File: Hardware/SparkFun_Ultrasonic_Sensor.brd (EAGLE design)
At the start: 45 x 21.5 mm, 61 parts, among them J4 Vertical Qwiic Connector, J6 Vertical Qwiic Connector, Q1 600mA/40V, U5 ULTRASONIC_SENSOR_TRANSMITTER, U6 LMV324, U7 STM8L051F3, U8 SP3232EB, U9 ULTRASONIC_SENSOR_RECEIVER

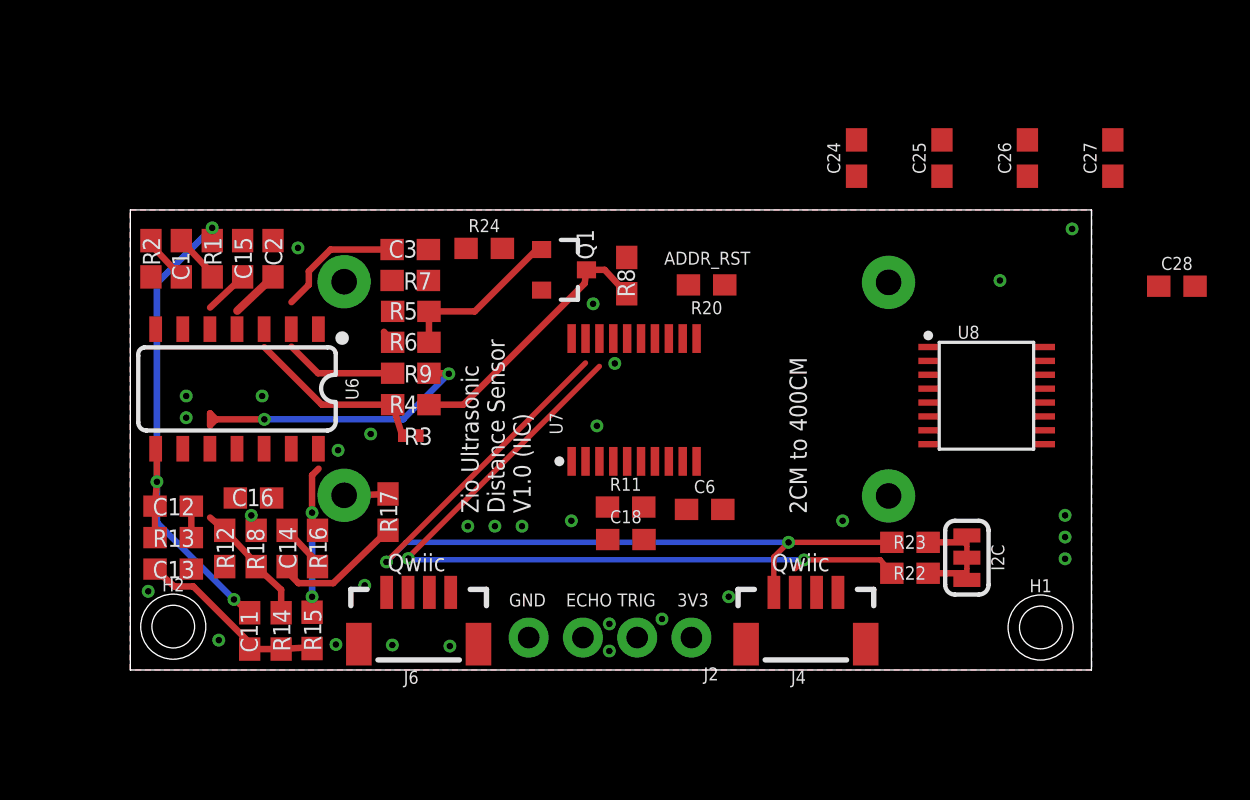
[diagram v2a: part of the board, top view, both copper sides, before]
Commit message: Moves passives around the PCB
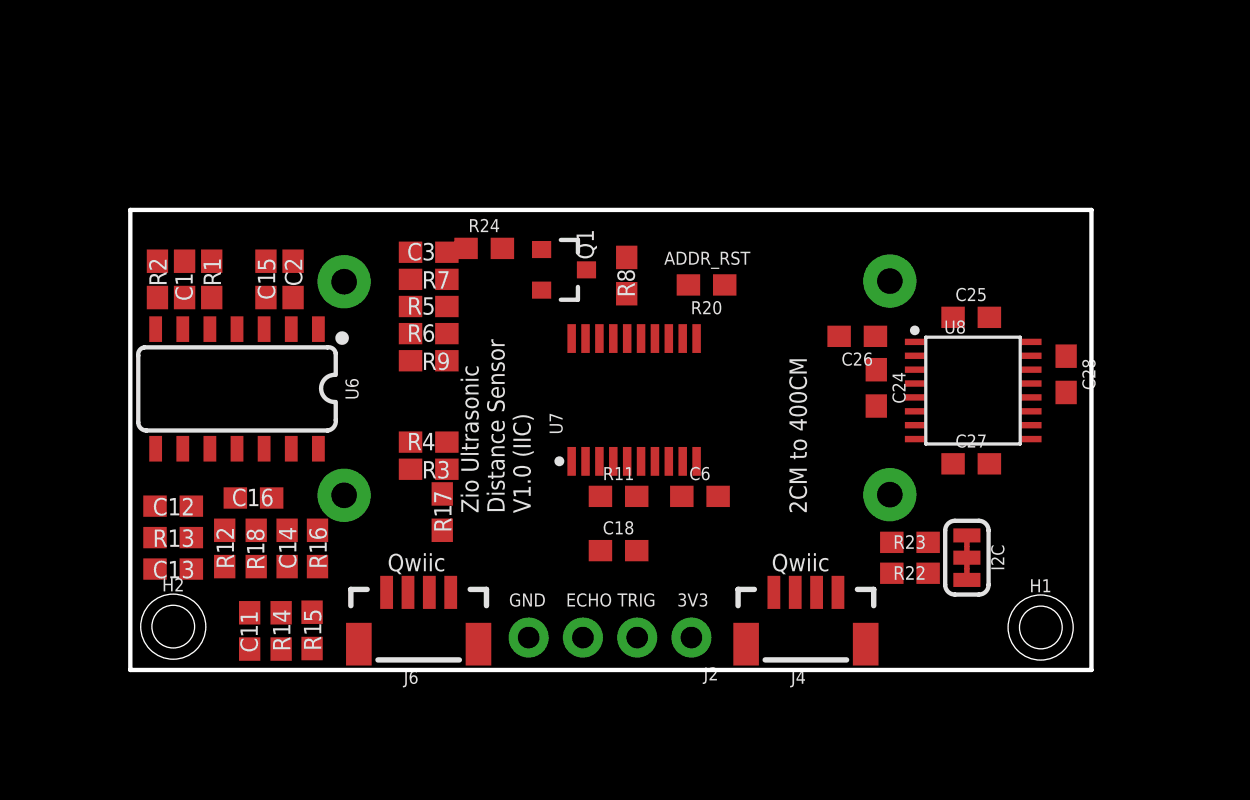
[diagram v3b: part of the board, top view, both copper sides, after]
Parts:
- R3: value 4.3k -> 4.7k; device SparkFun-Resistors:0402_MURATA -> SparkFun-Resistors:0603
- moved C27 15.8 mm to (39.4, 11.7), turned to 0 degrees
- moved C26 11.5 mm to (34.0, 17.7), turned to 180 degrees
- moved C24 10.8 mm to (34.9, 15.2), turned to 270 degrees
- moved C25 7.58 mm to (39.4, 18.5), turned to 0 degrees
- moved C28 6.63 mm to (43.8, 15.9), turned to 270 degrees
- moved R17 2.54 mm to (14.6, 9.42)
- moved R4 1.94 mm to (14.0, 12.7)
- moved R3 1.78 mm to (14.0, 11.4)
- moved C15 1.46 mm to (6.35, 20.3)
- moved C2 1.35 mm to (7.62, 20.3)
- moved R9 1.02 mm to (14.0, 16.5)
- moved R2 1.01 mm to (1.27, 20.3)
- moved C1 0.98 mm to (2.54, 20.3)
- moved R1 0.97 mm to (3.81, 20.3)
- moved R6 0.93 mm to (14.0, 17.8)
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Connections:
- net N$1: now also R3.1; no longer R3.P$1
- net N$4: now also R3.2; no longer R3.P$2
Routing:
- net SCL: track 39.8 -> 0.00 mm, vias 2 -> 0
- net SDA: track 36.3 -> 0.00 mm, vias 2 -> 0
- net N$10: track 25.4 -> 0.00 mm, vias 3 -> 0
- net N$31: track 22.5 -> 0.00 mm, vias 2 -> 0
- net INT: track 12.7 -> 0.00 mm
- net PB4: track 11.4 -> 0.00 mm
- net N$12: track 9.10 -> 0.00 mm
- net N$4: track 8.64 -> 0.00 mm
- net N$5: track 7.92 -> 0.00 mm
- net N$14: track 7.81 -> 0.00 mm, vias 2 -> 0
- net N$16: track 6.19 -> 0.00 mm
- net N$15: track 2.50 -> 0.00 mm
- net N$2: track 2.34 -> 0.00 mm
- net 3.3V: track 2.31 -> 0.00 mm
- net N$3: track 2.27 -> 0.00 mm
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
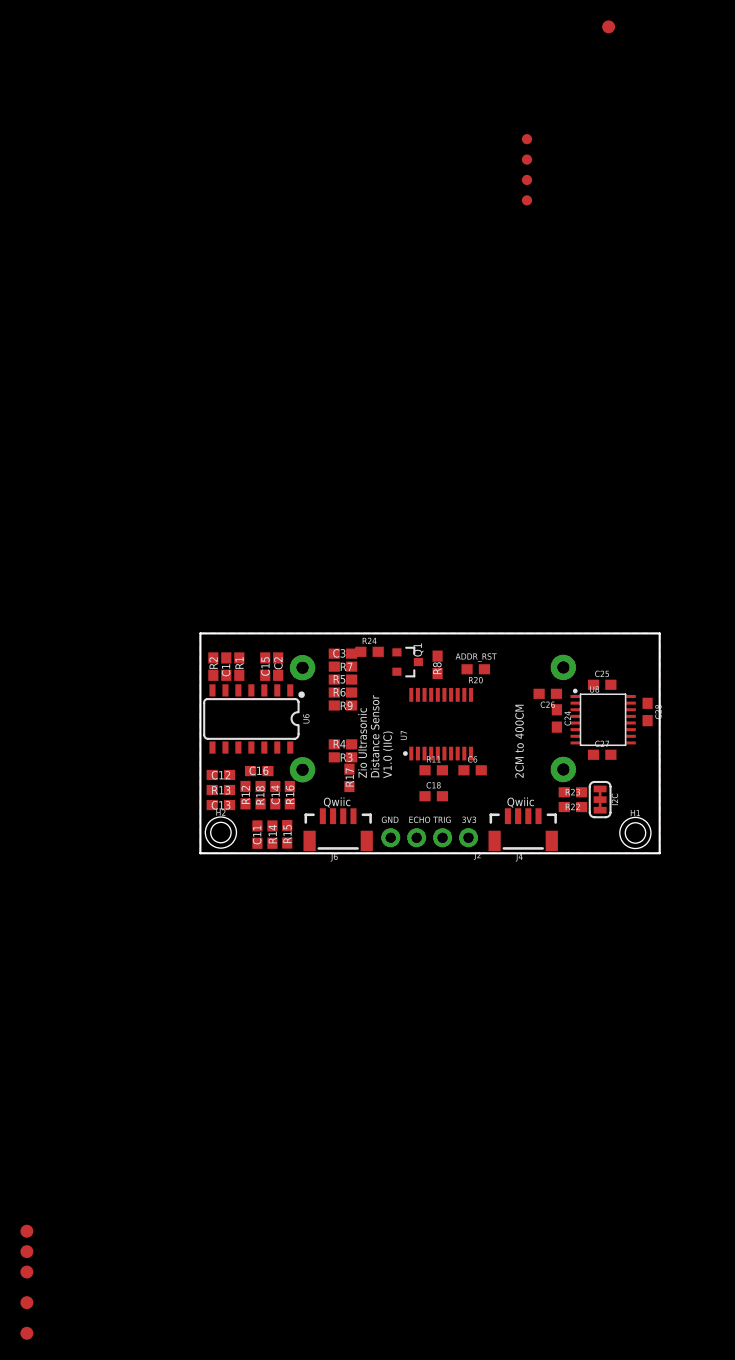
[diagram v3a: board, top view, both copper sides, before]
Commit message: Moves design to origin, routes most signals
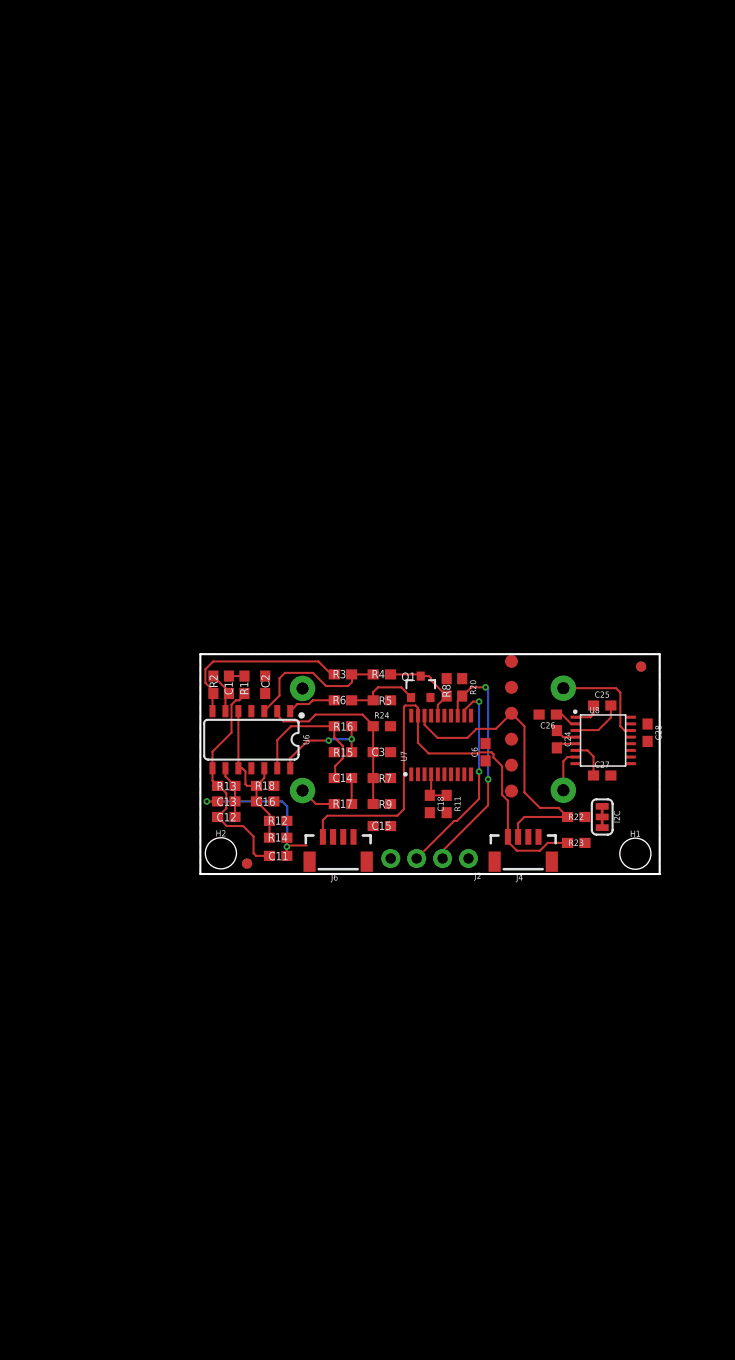
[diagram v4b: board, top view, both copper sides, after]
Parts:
- removed U$5: (no value), ZIO_silkscreen_package:6MM
- moved TP5 76.7 mm to (30.5, 18.3)
- moved FD1 76.1 mm to (4.57, 1.02), turned to 90 degrees
- moved TP6 75.1 mm to (30.5, 13.2)
- moved TP4 72.5 mm to (30.5, 15.7)
- moved FD4 70.5 mm to (4.57, 1.02), flipped to the bottom, turned to 90 degrees
- moved TP2 65.9 mm to (30.5, 10.7)
- moved TP3 65.5 mm to (30.5, 8.13)
- moved TP1 62.9 mm to (30.5, 20.8)
- moved FD2 50.9 mm to (43.2, 20.3), turned to 90 degrees
- moved FD3 49.0 mm to (43.2, 20.3), flipped to the bottom, turned to 90 degrees
- moved FRAME1 21.6 mm to (-7.16, -13.9)
- moved C15 19.4 mm to (17.8, 4.70), turned to 0 degrees
- moved R7 11.6 mm to (17.8, 9.40)
- moved R9 10.4 mm to (17.8, 6.86)
- moved C3 10.4 mm to (17.8, 11.9)
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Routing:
- net SCL: track 0.00 -> 48.7 mm
- net SDA: track 0.00 -> 30.9 mm
- net TRIG: track 0.00 -> 23.5 mm, vias 0 -> 2
- net N$10: track 0.00 -> 22.2 mm
- net ECHO: track 0.00 -> 20.4 mm, vias 0 -> 2
- net PB4: track 0.00 -> 18.5 mm
- net N$1: track 0.00 -> 17.9 mm
- net N$12: track 0.00 -> 16.9 mm, vias 0 -> 2
- net N$31: track 0.00 -> 16.5 mm
- net N$4: track 0.00 -> 14.7 mm
- net N$15: track 0.00 -> 14.7 mm
- net N$14: track 0.00 -> 10.3 mm, vias 0 -> 2
- net N$48: track 0.00 -> 10.3 mm
- net INT: track 0.00 -> 8.78 mm
- net N$5: track 0.00 -> 7.26 mm
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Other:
- board text removed: "2CM to 400CM"
- board text removed: "3V3"
- board text removed: "ADDR_RST"
- board text removed: "ECHO"
- board text removed: "GND"
- board text removed: "Qwiic"
- board text removed: "TRIG"
- board text removed: "Zio Ultrasonic Distance Sensor V1.0 (IIC)"

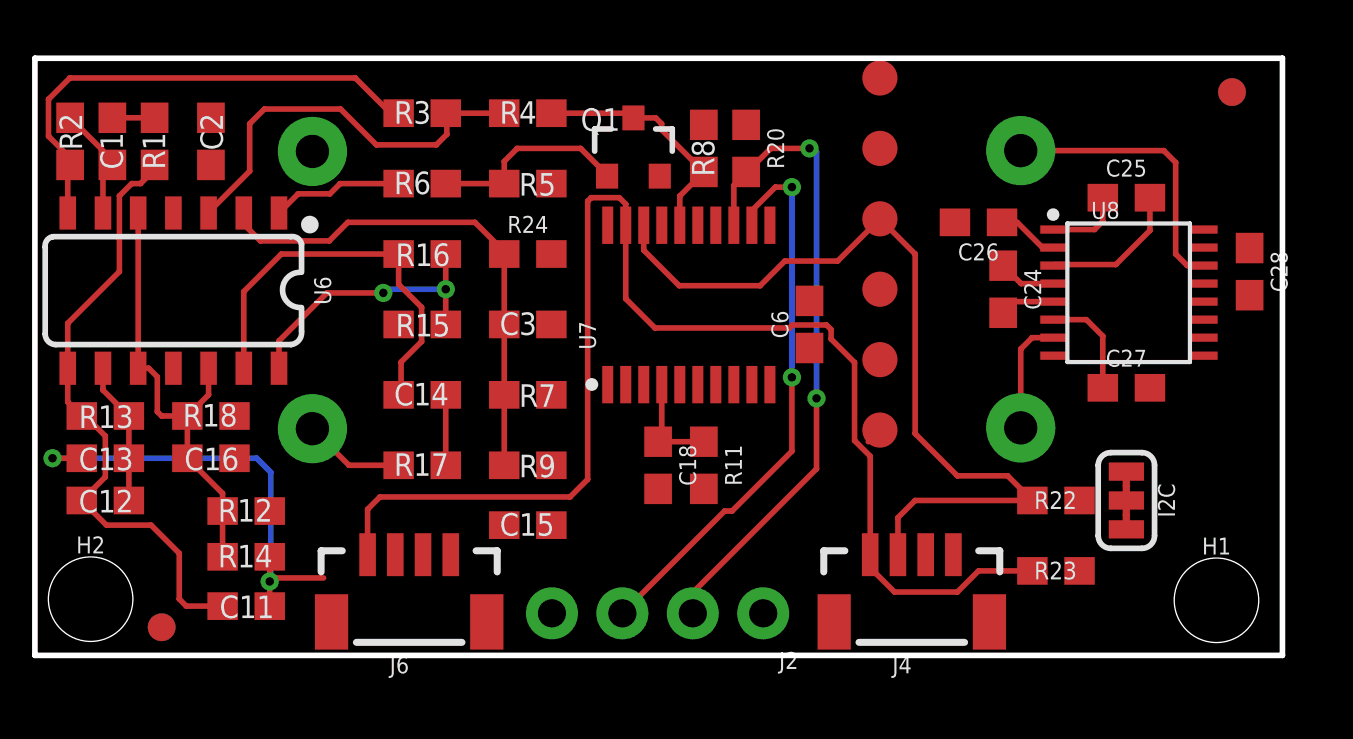
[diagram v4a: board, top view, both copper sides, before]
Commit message: Routes more wires
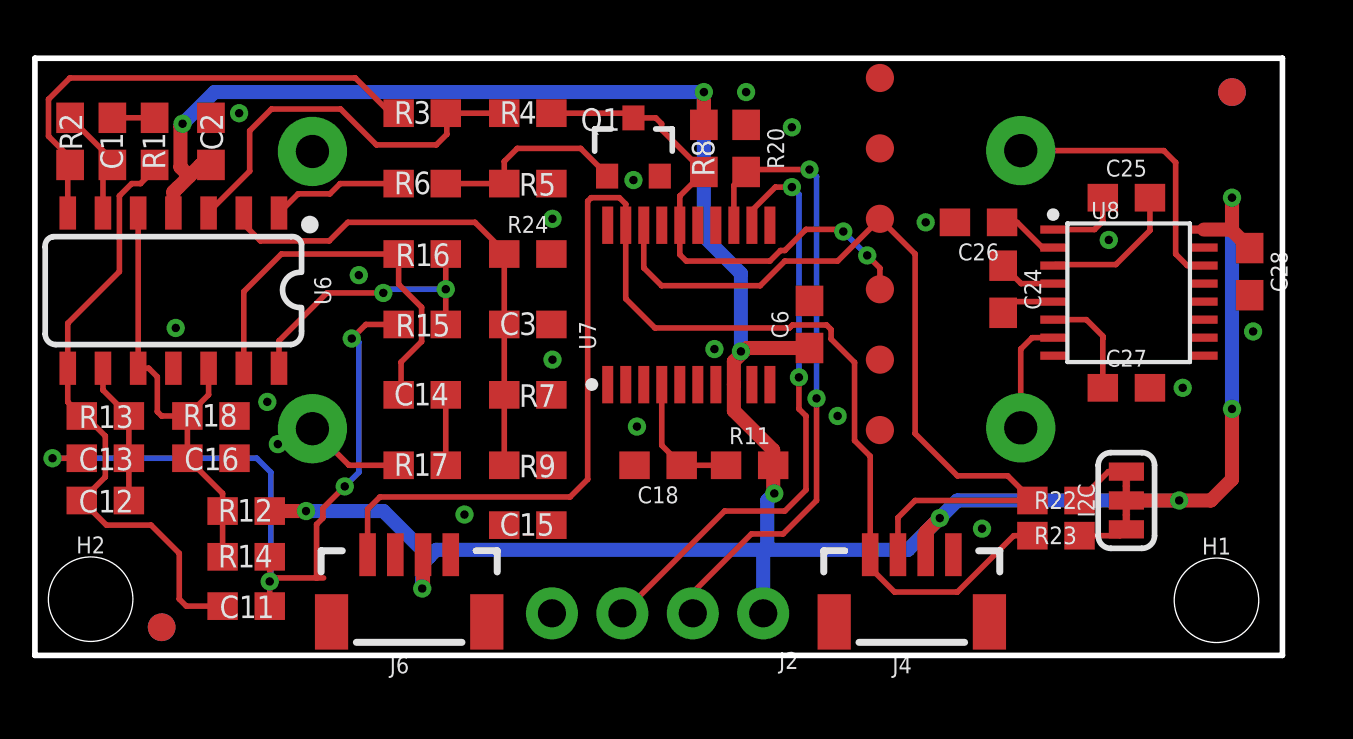
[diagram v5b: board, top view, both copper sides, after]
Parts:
- TP1, TP2, TP3, TP4, TP5, TP6: value TEST-POINT3X5 -> TEST-POINT3X4; device SparkFun-Connectors:PAD.03X.05 -> SparkFun-Connectors:PAD.03X.04
- moved R11 1.65 mm to (25.8, 6.86), turned to 0 degrees
- moved R23 1.27 mm to (36.8, 4.32)
- turned C18 to 180 degrees
- turned I2C to 90 degrees
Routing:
- net 3.3V: track 0.00 -> 103.6 mm, vias 0 -> 10
- net N$12: track 16.9 -> 28.2 mm, vias 2 -> 4
- net INT: track 8.78 -> 19.0 mm, vias 0 -> 2
- net N$19: track 0.00 -> 2.12 mm
- net N$20: track 0.00 -> 1.78 mm
- net ECHO: track 20.4 -> 21.9 mm
- net SCL: track 48.7 -> 49.2 mm

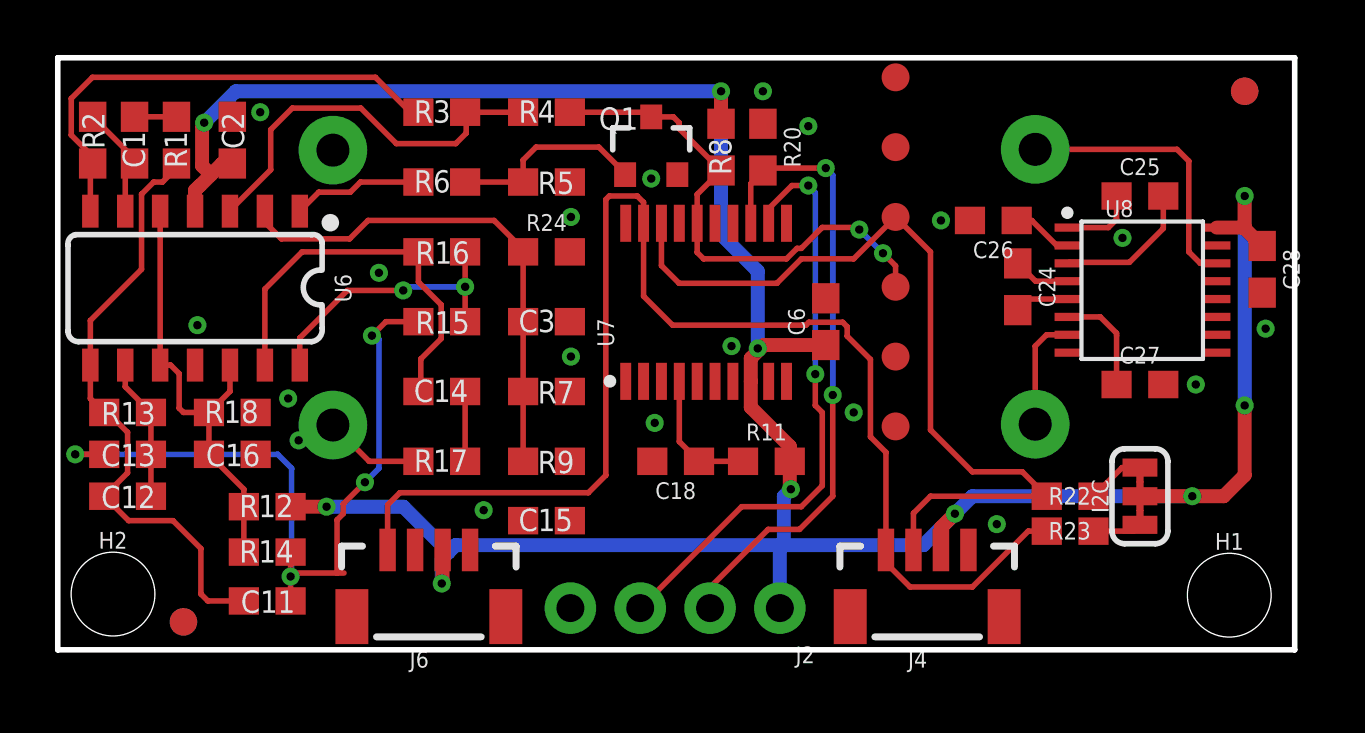
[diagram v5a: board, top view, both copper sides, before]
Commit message: Finishes routing the board.
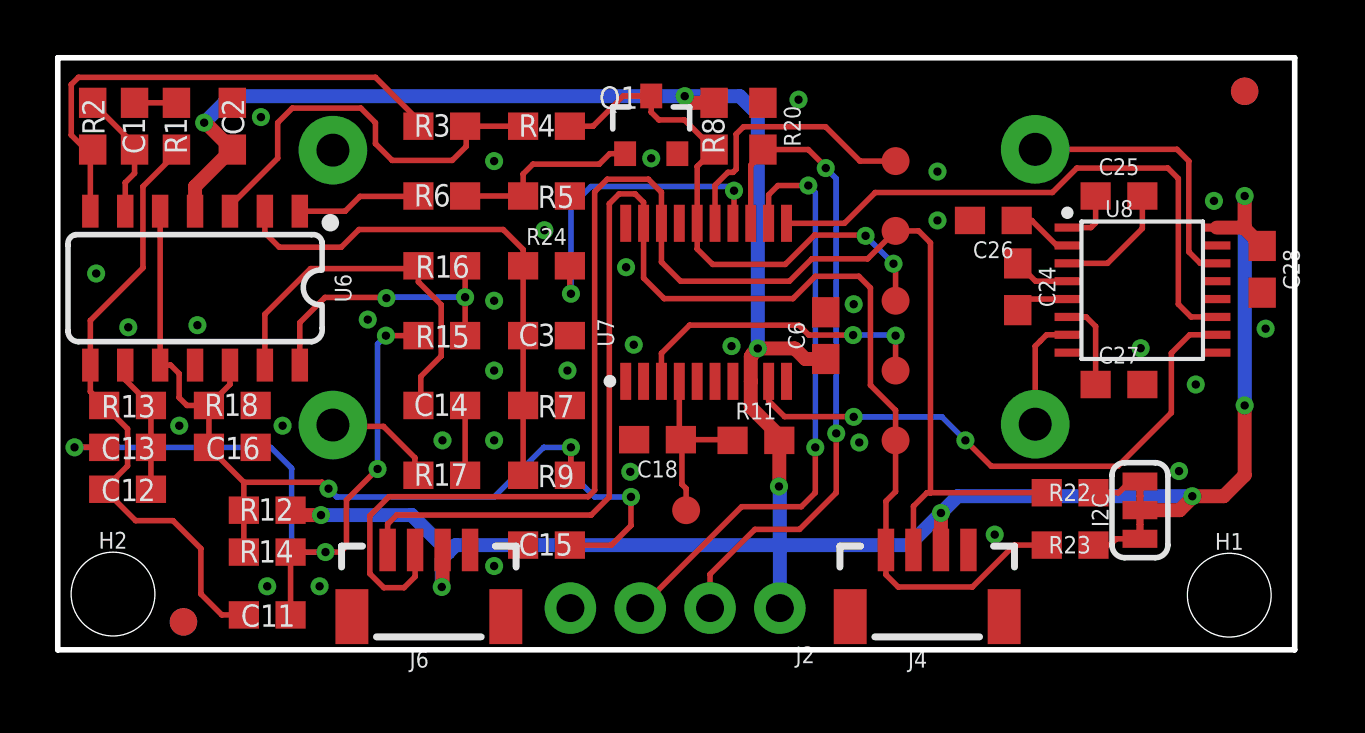
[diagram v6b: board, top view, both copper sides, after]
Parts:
- moved TP5 10.7 mm to (30.5, 7.62)
- moved TP3 8.21 mm to (22.9, 5.08)
- moved TP1 3.05 mm to (30.5, 17.8)
- moved C18 1.03 mm to (21.8, 7.65)
- moved C15 0.89 mm to (17.8, 3.81)
- moved R11 0.85 mm to (25.4, 7.62)
- moved R8 0.80 mm to (23.9, 19.1)
- moved C25 0.76 mm to (38.6, 16.5)
- moved C27 0.76 mm to (38.6, 9.65)
- moved Q1 0.76 mm to (21.6, 19.1)
- moved R20 0.76 mm to (25.7, 19.1)
- moved C3 0.51 mm to (17.8, 11.4)
- moved C6 0.51 mm to (27.9, 11.4)
- moved R15 0.51 mm to (14.0, 11.4)
- moved TP6 0.51 mm to (30.5, 12.7)
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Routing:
- net SDA: track 31.3 -> 56.6 mm
- net DIN1: track 0.00 -> 21.4 mm
- net DIN2: track 0.00 -> 21.2 mm, vias 0 -> 2
- net N$31: track 16.5 -> 37.1 mm, vias 0 -> 3
- net N: track 0.00 -> 11.7 mm, vias 0 -> 2
- net SWIM: track 0.00 -> 11.4 mm, vias 0 -> 2
- net ADDR_RST: track 0.00 -> 10.1 mm
- net NRST: track 4.81 -> 6.71 mm
- net SCL: track 49.2 -> 51.1 mm
- net TRIG: track 23.1 -> 24.5 mm
- net INT: track 19.0 -> 20.4 mm
- net N$12: track 28.2 -> 27.1 mm
- net N$1: track 17.9 -> 18.7 mm
- net N$37: track 5.16 -> 4.40 mm
- net N$15: track 14.7 -> 13.9 mm
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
